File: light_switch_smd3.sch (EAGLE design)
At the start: 26 parts, among them U1 ESP8266_ESP-01

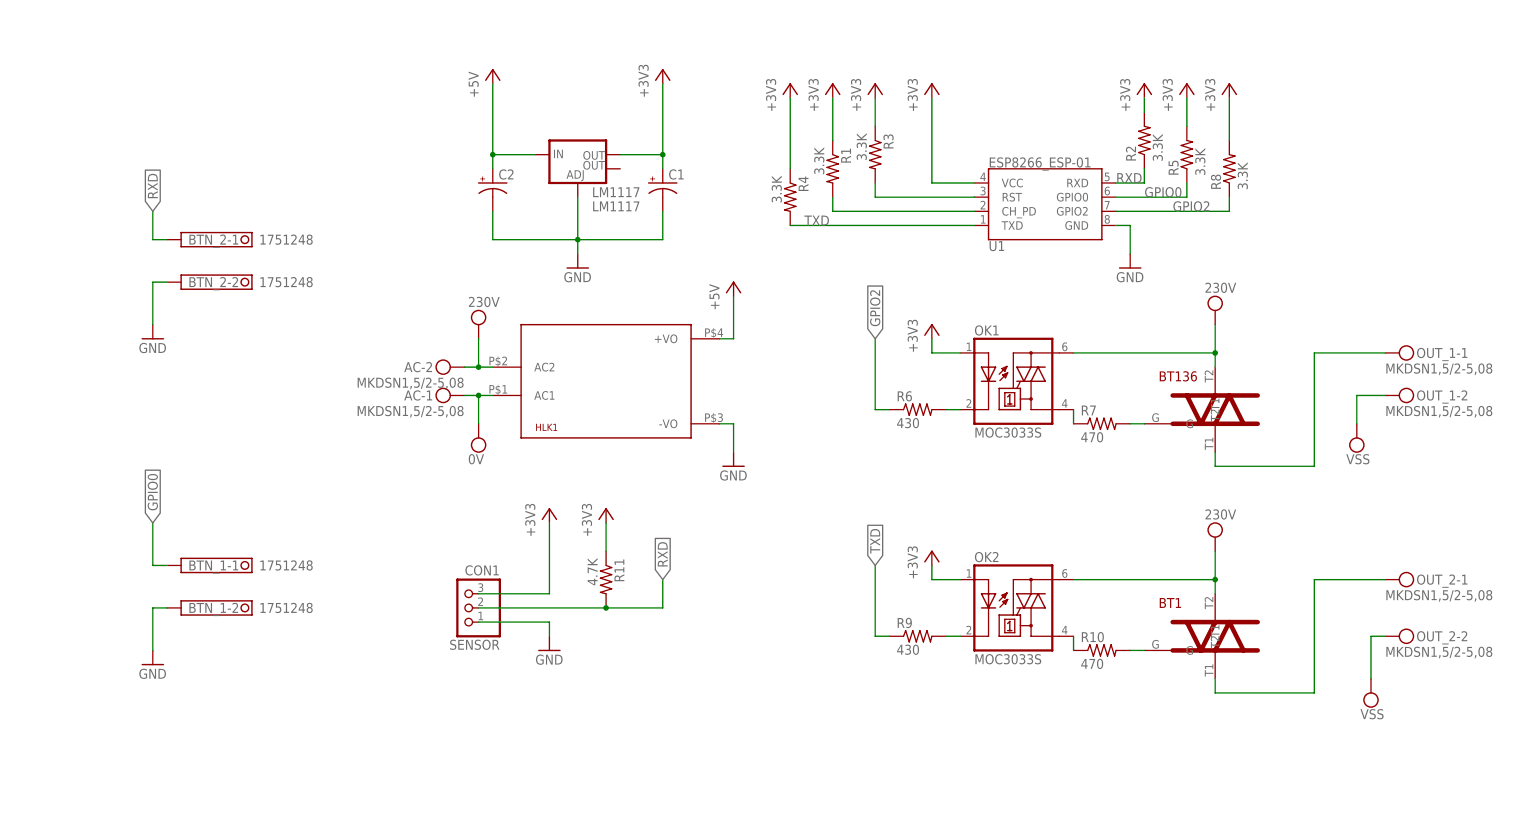
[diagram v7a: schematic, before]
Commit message: added LEDs, more rounded corners, +5V power connector
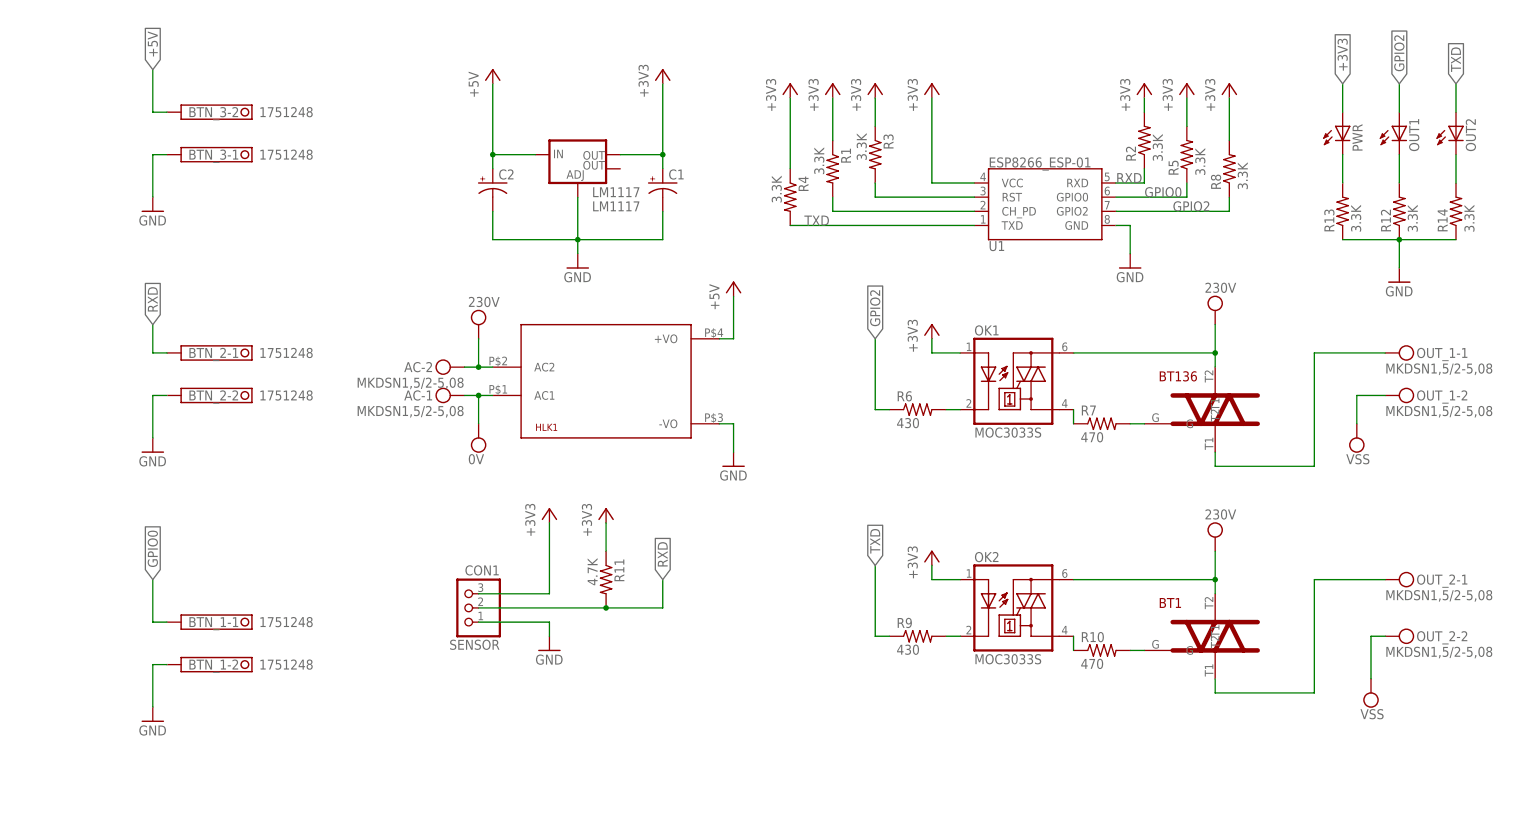
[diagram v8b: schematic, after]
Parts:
- added BTN_3: 1751248, con-phoenix-350:1751248
- added OUT1, OUT2, PWR: (no value), led:LEDSML1206
- added R12, R13, R14: 3.3K, resistor:R-US_R1206
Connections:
- new net N$1: PWR.C, R13.2
- new net N$11: OUT2.C, R14.2
- new net N$9: OUT1.C, R12.2
- net +3V3: now also PWR.A
- net +5V: now also BTN_3-2.K
- net GND: now also BTN_3-1.K, R12.1, R13.1, R14.1
- net GPIO2: now also OUT1.A
- net TXD: now also OUT2.A
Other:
- moved on the sheet: BTN_1-1, BTN_1-2, BTN_2-1, BTN_2-2
